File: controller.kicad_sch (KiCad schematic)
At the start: 33 parts, among them J10 07x01_2.54mm_Header, J4 03x01_2.54mm_Header, J6 03x01_2.54mm_Header, J9 07x01_2.54mm_Header, U4 STM32H742VGT6

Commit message: updates components to latest library. Refs: #30
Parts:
- U4: footprint Package_QFP:LQFP-100_14x14mm_P0.5mm -> KL_Footprints:LQFP-100_14x14mm_P0.5mm
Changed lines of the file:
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@@
 		(on_board yes)
 		(dnp no)
+		(fields_autoplaced yes)
 		(property "Reference" "J4"
-			(at 190.246 74.676 0)
+			(at 190.5 63.5 0)
 			(effects
 				(font
@@
 			)
 		)
-		(property "Dielectric" ""
-			(at 69.85 133.35 90)
-			(effects
-				(font
-					(size 1.27 1.27)
-				)
-				(hide yes)
-			)
-		)
-		(property "Dielectric_type" ""
-			(at 69.85 133.35 90)
-			(effects
-				(font
-					(size 1.27 1.27)
-				)
-				(hide yes)
-			)
-		)
-		(property "LSCS" ""
-			(at 69.85 133.35 90)
-			(effects
-				(font
-					(size 1.27 1.27)
-				)
-				(hide yes)
-			)
-		)
-		(property "Max Current" ""
-			(at 69.85 133.35 90)
-			(effects
-				(font
-					(size 1.27 1.27)
-				)
-				(hide yes)
-			)
-		)
 		(pin "2"
 		)
@@
 		(fields_autoplaced yes)
 		(property "Reference" "J10"
-			(at 214.63 67.31 0)
+			(at 212.09 77.7874 0)
 			(effects
 				(font
 					(size 1.27 1.27)
 				)
+				(justify left)
 			)
 		)
@@
 			)
 		)
-		(property "Dielectric" ""
-			(at 69.85 148.59 90)
-			(effects
-				(font
-					(size 1.27 1.27)
-				)
-				(hide yes)
-			)
-		)
-		(property "Dielectric_type" ""
-			(at 69.85 148.59 90)
-			(effects
-				(font
-					(size 1.27 1.27)
-				)
-				(hide yes)
-			)
-		)
-		(property "LSCS" ""
-			(at 69.85 148.59 90)
-			(effects
-				(font
-					(size 1.27 1.27)
-				)
-				(hide yes)
-			)
-		)
-		(property "Max Current" ""
-			(at 69.85 148.59 90)
-			(effects
-				(font
-					(size 1.27 1.27)
-				)
-				(hide yes)
-			)
-		)
 		(pin "2"
 		)
@@
 		)
 		(property "LABEL" "${REFERENCE}:${COLOR}"
-			(at 58.42 129.794 0)
+			(at 58.166 135.89 0)
 			(effects
 				(font
@@
 		)
 		(property "LABEL" "${REFERENCE}:${COLOR}"
-			(at 58.42 144.78 0)
+			(at 58.166 151.13 0)
 			(effects
 				(font
@@
 			)
 		)
-		(property "Footprint" "Package_QFP:LQFP-100_14x14mm_P0.5mm"
+		(property "Footprint" "KL_Footprints:LQFP-100_14x14mm_P0.5mm"
 			(at 83.82 173.99 0)
 			(effects
@@
 		(fields_autoplaced yes)
 		(property "Reference" "J9"
-			(at 214.63 48.26 0)
+			(at 212.09 58.7374 0)
 			(effects
 				(font
 					(size 1.27 1.27)
 				)
+				(justify left)
 			)
 		)
@@
 		(dnp no)
 		(fields_autoplaced yes)
-		(property "Reference" "#PWR095"
+		(property "Reference" "#PWR95"
 			(at 45.72 144.78 0)
 			(effects
@@
 			(project ""
 				(path "/d4536448-b109-4159-96e2-3dc21baf2d6e/06488c82-a47f-4277-b0ee-3bd211d8922a"
-					(reference "#PWR095")
+					(reference "#PWR95")
 					(unit 1)
 				)
@@
 		)
 		(property "LABEL" "${REFERENCE}:${COLOR}"
-			(at 58.42 137.16 0)
+			(at 58.166 143.51 0)
 			(effects
 				(font
@@
 			(effects
 				(font
-					(size 1.27 1.27)
-				)
-				(hide yes)
-			)
-		)
-		(property "Dielectric" ""
-			(at 69.85 140.97 90)
-			(effects
-				(font
-					(size 1.27 1.27)
-				)
-				(hide yes)
-			)
-		)
-		(property "Dielectric_type" ""
-			(at 69.85 140.97 90)
-			(effects
-				(font
-					(size 1.27 1.27)
-				)
-				(hide yes)
-			)
-		)
-		(property "LSCS" ""
-			(at 69.85 140.97 90)
-			(effects
-				(font
-					(size 1.27 1.27)
-				)
-				(hide yes)
-			)
-		)
-		(property "Max Current" ""
-			(at 69.85 140.97 90)
-			(effects
-				(font

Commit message: open project in KiCAD10. Refs: #41
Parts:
- TP23, TP32, TP33, TP34, TP35: value ~ -> (none)

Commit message: updates controller. Refs: #41
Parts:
- C104, C77, C78, C85, C93, C94, C95: symbol KL_C:C_100n_10V_X7R_0603_10 -> KL_C:C_100n_10V_10pct_X7R_0603; Dielectric (none) -> X7R; MPN (none) -> CC0603KRX7R6BB104; Package_in_inch (none) -> 0603; Tolerance 10 -> (none); Tolerance_in_pct (none) -> 10; Voltage 50 -> (none); Voltage_in_V (none) -> 10
- C105: symbol KL_C:C_4u7_10V_X5R_0603_10 -> KL_C:C_4u7_10V_10pct_X5R_0603; Dielectric (none) -> X5R; MPN (none) -> C0603C475K8PAC7411; Package_in_inch (none) -> 0603; Tolerance 10 -> (none); Tolerance_in_pct (none) -> 10; Voltage 10 -> (none); Voltage_in_V (none) -> 10
- C81, C82, C83, C84: symbol KL_C:C_2u2_10V_Y5V_0603_20 -> KL_C:C_2u2_10V_20pct_Y5V_0603; Dielectric (none) -> Y5V; MPN (none) -> EMK107BJ225KA-T; Package_in_inch (none) -> 0603; Tolerance 10 -> (none); Tolerance_in_pct (none) -> 20; Voltage 16 -> (none); Voltage_in_V (none) -> 10
- D4: symbol KL_LED:LED_green_2V1_0.03A -> KL_LED:LED_Green_2.1V_0.03A_0603; MPN (none) -> LTST-C190GKT; Package_in_inch (none) -> 0603
- D5: symbol KL_LED:LED_orange_2V_0.03A -> KL_LED:LED_Orange_2V_0.03A_0603; MPN (none) -> LTST-C190KFKT; Package_in_inch (none) -> 0603
- D6: symbol KL_LED:LED_red_2V_0.03A -> KL_LED:LED_Red_2V_0.03A_0603; MPN (none) -> LTST-C194KRKT; Package_in_inch (none) -> 0603
- J10, J9: value 07x01_2.54mm_Header -> Header_07x01_2.54mm_0mm_Straight; symbol KL_Headers:07x01_2.54mm_Header -> KL_Header:Header_07x01_2.54mm_0mm_Straight; MPN (none) -> TLW-107-06-G-S; No_of_pins (none) -> 7; No_of_rows (none) -> 1; Orientation (none) -> Straight; Pitch_pin_in_mm (none) -> 2.54; Pitch_row_in_mm (none) -> 0
- J4, J6: value 03x01_2.54mm_Header -> Header_03x01_2.54mm_0mm_Straight; symbol KL_Headers:03x01_2.54mm_Header -> KL_Header:Header_03x01_2.54mm_0mm_Straight; MPN (none) -> 87224-3; No_of_pins (none) -> 3; No_of_rows (none) -> 1; Orientation (none) -> Straight; Pitch_pin_in_mm (none) -> 2.54; Pitch_row_in_mm (none) -> 0
- R102: symbol KL_R:R_10K_100mW_5_0603 -> KL_R:R_10K_0.1W_5pct_0603; MPN (none) -> CRCW060310K0JNEC; Package (in) 0603 -> (none); Package_in_inch (none) -> 0603; Power 100mW -> (none); Power_in_W (none) -> 0.1; Tolerance 5% -> (none); Tolerance_in_pct (none) -> 5
- R108: symbol KL_R:R_0R_2W_5_2512 -> KL_R:R_0R_2W_5pct_2512; MPN (none) -> CRF2512-J/-000ELF; Mouser 652-CRF2512-J-000ELF -> 652-CRF2512-J-000ELF; Package (in) 2512 -> (none); Package_in_inch (none) -> 2512; Power 2 -> (none); Power_in_W (none) -> 2; Tolerance 5 -> (none); Tolerance_in_pct (none) -> 5
- R110, R111, R74: value 22 -> 22R; symbol KL_R:R_22_100mW_1pct_0603 -> KL_R:R_22R_0.1W_1pct_0603; MPN (none) -> RC0603FR-1022RL; Package (in) 0603 -> (none); Package_in_inch (none) -> 0603; Power 0.1 -> (none); Power_in_W (none) -> 0.1; Tolerance 1 -> (none); Tolerance_in_pct (none) -> 1
- R137, R87, R89: symbol KL_R:R_1K5_100mW_5_0603 -> KL_R:R_1K5_0.1W_5pct_0603; MPN (none) -> AC0603JR-071K5L; Package (in) 0603 -> (none); Package_in_inch (none) -> 0603; Power 0.1 -> (none); Power_in_W (none) -> 0.1; Tolerance 5 -> (none); Tolerance_in_pct (none) -> 5
- TP23, TP32, TP33, TP34, TP35: footprint Connector_PinHeader_2.54mm:PinHeader_1x01_P2.54mm_Vertical -> KL_Footprints:TestPoint; symbol KL_TP:TestPoint -> KL_TestPoint:TestPoint
- U4: MPN (none) -> STM32H742VGT6; V_DD_max_V (none) -> 4

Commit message: updates 2u2 capacitors. Refs: #41
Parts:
- C81, C82, C83, C84: symbol KL_C:C_2u2_10V_20pct_Y5V_0603 -> KL_C:C_2u2_35V_20pct_X5R_0603; Dielectric Y5V -> X5R; Digikey 587-1430-1-ND -> 490-10486-1-ND; LCSC C76612 -> C710921; MPN EMK107BJ225KA-T -> GRM188R6YA225MA12D; Mouser 963-EMK107BJ225KA-T -> 81-GRM188R6YA225MA2D; Voltage_in_V 10 -> 35
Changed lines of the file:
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@@
 	)
 	(symbol
-		(lib_id "KL_C:C_2u2_10V_20pct_Y5V_0603")
+		(lib_id "KL_C:C_2u2_35V_20pct_X5R_0603")
 		(at 29.21 173.99 90)
 		(unit 1)
@@
 			)
 		)
-		(property "Datasheet" "file:///home/alex/Downloads/MLASE168SB5225KTNA01_SS.pdf"
+		(property "Datasheet" "https://search.murata.co.jp/Ceramy/image/img/A01X/G101/ENG/GRM188R6YA225MA12-01.pdf"
 			(at 29.21 173.99 0)
 			(hide yes)
@@
 			)
 		)
-		(property "Mouser" "963-EMK107BJ225KA-T"
+		(property "Mouser" "81-GRM188R6YA225MA2D"
 			(at 29.21 173.99 0)
 			(hide yes)
@@
 			)
 		)
-		(property "Digikey" "587-1430-1-ND"
+		(property "Digikey" "490-10486-1-ND"
 			(at 29.21 173.99 0)
 			(hide yes)
@@
 			)
 		)
-		(property "LCSC" "C76612"
+		(property "LCSC" "C710921"
 			(at 29.21 173.99 0)
 			(hide yes)
@@
 			)
 		)
-		(property "Voltage_in_V" "10"
+		(property "Voltage_in_V" "35"
 			(at 29.21 173.99 0)
 			(hide yes)
@@
 			)
 		)
-		(property "Dielectric" "Y5V"
+		(property "Dielectric" "X5R"
 			(at 29.21 173.99 0)
 			(hide yes)
@@
 			)
 		)
-		(property "MPN" "EMK107BJ225KA-T"
+		(property "MPN" "GRM188R6YA225MA12D"
 			(at 29.21 173.99 0)
 			(hide yes)
@@
 	)
 	(symbol
-		(lib_id "KL_C:C_2u2_10V_20pct_Y5V_0603")
+		(lib_id "KL_C:C_2u2_35V_20pct_X5R_0603")
 		(at 29.21 162.56 90)
 		(unit 1)
@@
 			)
 		)
-		(property "Datasheet" "file:///home/alex/Downloads/MLASE168SB5225KTNA01_SS.pdf"
+		(property "Datasheet" "https://search.murata.co.jp/Ceramy/image/img/A01X/G101/ENG/GRM188R6YA225MA12-01.pdf"
 			(at 29.21 162.56 0)
 			(hide yes)
@@
 			)
 		)
-		(property "Mouser" "963-EMK107BJ225KA-T"
+		(property "Mouser" "81-GRM188R6YA225MA2D"
 			(at 29.21 162.56 0)
 			(hide yes)
@@
 			)
 		)
-		(property "Digikey" "587-1430-1-ND"
+		(property "Digikey" "490-10486-1-ND"
 			(at 29.21 162.56 0)
 			(hide yes)
@@
 			)
 		)
-		(property "LCSC" "C76612"
+		(property "LCSC" "C710921"
 			(at 29.21 162.56 0)
 			(hide yes)
@@
 			)
 		)
-		(property "Voltage_in_V" "10"
+		(property "Voltage_in_V" "35"
 			(at 29.21 162.56 0)
 			(hide yes)
@@
 			)
 		)
-		(property "Dielectric" "Y5V"
+		(property "Dielectric" "X5R"
 			(at 29.21 162.56 0)
 			(hide yes)
@@
 			)
 		)
-		(property "MPN" "EMK107BJ225KA-T"
+		(property "MPN" "GRM188R6YA225MA12D"
 			(at 29.21 162.56 0)
 			(hide yes)
@@
 	)
 	(symbol
-		(lib_id "KL_C:C_2u2_10V_20pct_Y5V_0603")
+		(lib_id "KL_C:C_2u2_35V_20pct_X5R_0603")
 		(at 29.21 139.7 90)
 		(unit 1)
@@
 			)
 		)
-		(property "Datasheet" "file:///home/alex/Downloads/MLASE168SB5225KTNA01_SS.pdf"
+		(property "Datasheet" "https://search.murata.co.jp/Ceramy/image/img/A01X/G101/ENG/GRM188R6YA225MA12-01.pdf"
 			(at 29.21 139.7 0)
 			(hide yes)
@@
 			)
 		)
-		(property "Mouser" "963-EMK107BJ225KA-T"
+		(property "Mouser" "81-GRM188R6YA225MA2D"
 			(at 29.21 139.7 0)
 			(hide yes)
@@
 			)
 		)
-		(property "Digikey" "587-1430-1-ND"
+		(property "Digikey" "490-10486-1-ND"
 			(at 29.21 139.7 0)
 			(hide yes)
@@
 			)
 		)
-		(property "LCSC" "C76612"
+		(property "LCSC" "C710921"
 			(at 29.21 139.7 0)
 			(hide yes)
@@
 			)
 		)
-		(property "Voltage_in_V" "10"
+		(property "Voltage_in_V" "35"
 			(at 29.21 139.7 0)
 			(hide yes)
@@
 			)
 		)
-		(property "Dielectric" "Y5V"
+		(property "Dielectric" "X5R"
 			(at 29.21 139.7 0)
 			(hide yes)
@@
 			)
 		)
-		(property "MPN" "EMK107BJ225KA-T"
+		(property "MPN" "GRM188R6YA225MA12D"
 			(at 29.21 139.7 0)
 			(hide yes)
@@
 	)
 	(symbol
-		(lib_id "KL_C:C_2u2_10V_20pct_Y5V_0603")
+		(lib_id "KL_C:C_2u2_35V_20pct_X5R_0603")
 		(at 29.21 151.13 90)
 		(unit 1)
@@
 			)
 		)
-		(property "Datasheet" "file:///home/alex/Downloads/MLASE168SB5225KTNA01_SS.pdf"
+		(property "Datasheet" "https://search.murata.co.jp/Ceramy/image/img/A01X/G101/ENG/GRM188R6YA225MA12-01.pdf"
 			(at 29.21 151.13 0)
 			(hide yes)
@@
 			)
 		)
-		(property "Mouser" "963-EMK107BJ225KA-T"
+		(property "Mouser" "81-GRM188R6YA225MA2D"
 			(at 29.21 151.13 0)
 			(hide yes)
@@
 			)
 		)
-		(property "Digikey" "587-1430-1-ND"
+		(property "Digikey" "490-10486-1-ND"
 			(at 29.21 151.13 0)
 			(hide yes)
@@
 			)
 		)
-		(property "LCSC" "C76612"
+		(property "LCSC" "C710921"
 			(at 29.21 151.13 0)
 			(hide yes)
@@
 			)
 		)
-		(property "Voltage_in_V" "10"
+		(property "Voltage_in_V" "35"
 			(at 29.21 151.13 0)
 			(hide yes)
@@
 			)
 		)
-		(property "Dielectric" "Y5V"
+		(property "Dielectric" "X5R"
 			(at 29.21 151.13 0)
 			(hide yes)
@@
 			)
 		)
-		(property "MPN" "EMK107BJ225KA-T"
+		(property "MPN" "GRM188R6YA225MA12D"
 			(at 29.21 151.13 0)
 			(hide yes)

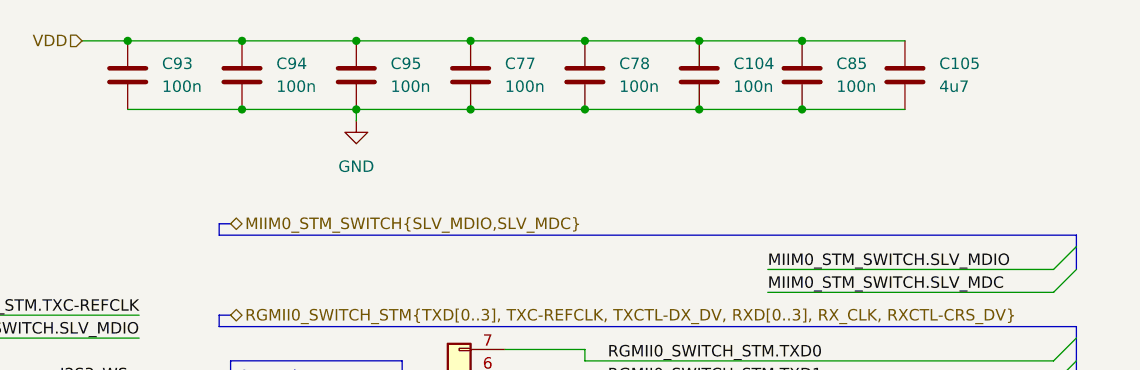
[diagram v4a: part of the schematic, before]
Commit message: replaces all capacitors with 10u. Refs: #52
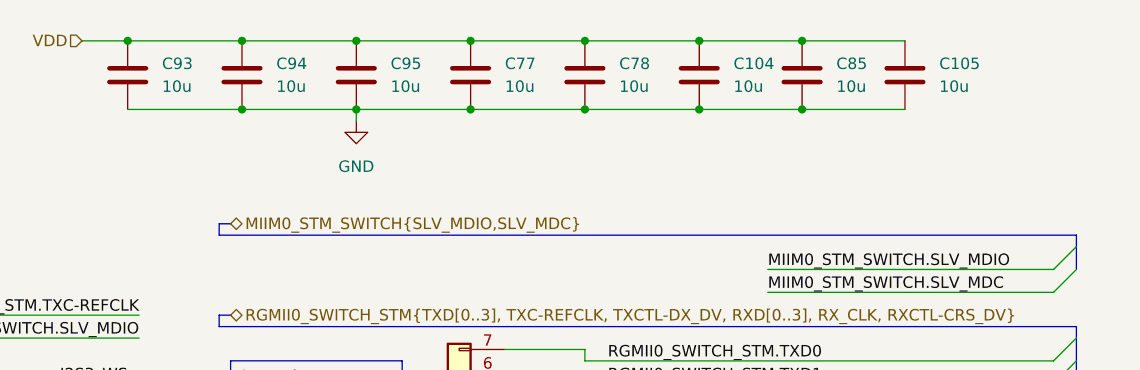
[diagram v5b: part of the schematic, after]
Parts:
- C104, C77, C78, C85, C93, C94, C95: value 100n -> 10u; symbol KL_C:C_100n_10V_10pct_X7R_0603 -> KL_C:C_10u_25V_20pct_X5R_0603; Dielectric X7R -> X5R; Digikey 311-4055-1-ND -> 1276-1869-1-ND; LCSC C519438 -> C96446; MPN CC0603KRX7R6BB104 -> CL10A106MA8NRNC; Mouser 603-CC603KRX7R6BB104 -> 187-CL10A106MA8NRNC; Tolerance_in_pct 10 -> 20; Voltage_in_V 10 -> 25
- C105: value 4u7 -> 10u; symbol KL_C:C_4u7_10V_10pct_X5R_0603 -> KL_C:C_10u_25V_20pct_X5R_0603; Digikey 399-C0603C475K8PACTUCT-ND -> 1276-1869-1-ND; LCSC C5177163 -> C96446; MPN C0603C475K8PAC7411 -> CL10A106MA8NRNC; Mouser 80-C0603C475K8PACLR -> 187-CL10A106MA8NRNC; Tolerance_in_pct 10 -> 20; Voltage_in_V 10 -> 25

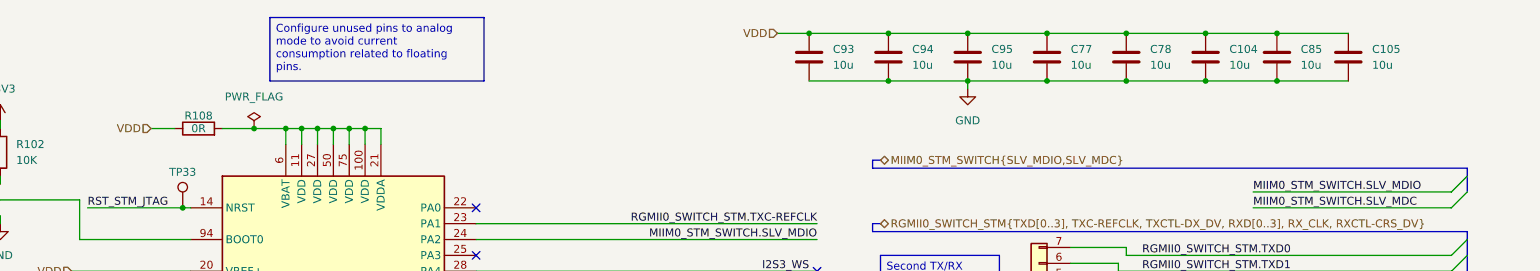
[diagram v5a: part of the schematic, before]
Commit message: moves 0R resistor in front of buffering caps. Refs: #57
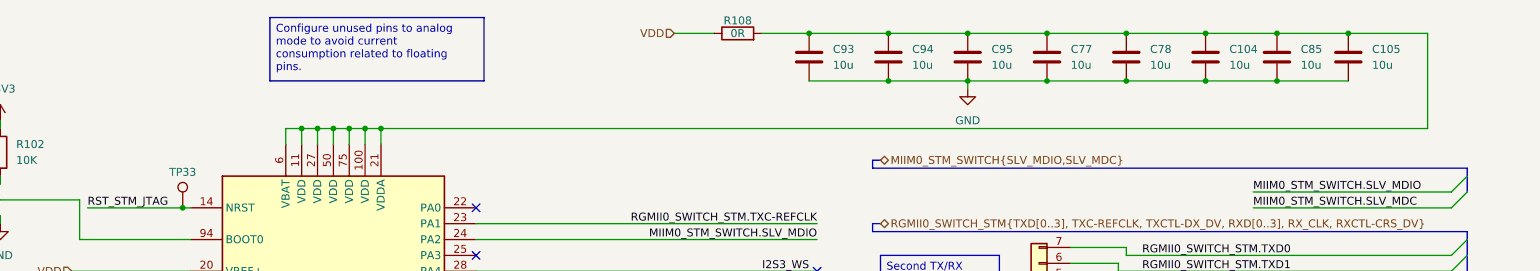
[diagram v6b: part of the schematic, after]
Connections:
- net VDD: no longer C104.1, C105.1, C77.1, C78.1, C85.1, C93.1, C94.1, C95.1
- net at R108.2, U4.100 (VDD), U4.11 (VDD)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: now also C104.1, C105.1, C77.1, C78.1, C85.1, C93.1, C94.1, C95.1
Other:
- moved on the sheet: R108
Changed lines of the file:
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@@
 	)
 	(junction
+		(at 177.8 16.51)
+		(diameter 0)
+		(color 0 0 0 0)
+	)
+	(junction
 		(at 99.06 181.61)
 		(diameter 0)
@@
 	)
 	(junction
+		(at 264.16 16.51)
+		(diameter 0)
+		(color 0 0 0 0)
+	)
+	(junction
 		(at 215.9 16.51)
 		(diameter 0)
@@
 	)
 	(junction
-		(at 177.8 16.51)
-		(diameter 0)
-		(color 0 0 0 0)
-	)
-	(junction
 		(at 228.6 16.51)
 		(diameter 0)
@@
 	)
 	(junction
-		(at 93.98 31.75)
+		(at 109.22 31.75)
 		(diameter 0)
 		(color 0 0 0 0)
@@
 	)
 	(junction
-		(at 88.9 31.75)
-		(diameter 0)
-		(color 0 0 0 0)
-	)
-	(junction
 		(at 101.6 31.75)
 		(diameter 0)
@@
 	(wire
 		(pts
+			(xy 109.22 31.75) (xy 276.86 31.75)
+		)
+		(stroke
+			(width 0)
+			(type default)
+		)
+	)
+	(wire
+		(pts
 			(xy 248.92 41.91) (xy 280.67 41.91)
 		)
@@
 	(wire
 		(pts
+			(xy 276.86 16.51) (xy 264.16 16.51)
+		)
+		(stroke
+			(width 0)
+			(type default)
+		)
+	)
+	(wire
+		(pts
 			(xy 78.74 156.21) (xy 33.02 156.21)
 		)
@@
 	(wire
 		(pts
-			(xy 72.39 31.75) (xy 76.2 31.75)
-		)
-		(stroke
-			(width 0)
-			(type default)
-		)
-	)
-	(wire
-		(pts
 			(xy 124.46 74.93) (xy 180.34 74.93)
 		)
@@
 	(wire
 		(pts
+			(xy 276.86 31.75) (xy 276.86 16.51)
+		)
+		(stroke
+			(width 0)
+			(type default)
+		)
+	)
+	(wire
+		(pts
 			(xy 124.46 140.97) (xy 179.07 140.97)
 		)
@@
 	(wire
 		(pts
+			(xy 170.18 16.51) (xy 177.8 16.51)
+		)
+		(stroke
+			(width 0)
+			(type default)
+		)
+	)
+	(wire
+		(pts
 			(xy 222.25 133.35) (xy 248.92 133.35)
 		)
@@
 	(wire
 		(pts
-			(xy 172.72 16.51) (xy 177.8 16.51)
+			(xy 156.21 16.51) (xy 162.56 16.51)
 		)
 		(stroke
@@
 	(wire
 		(pts
-			(xy 83.82 31.75) (xy 88.9 31.75)
-		)
-		(stroke
-			(width 0)
-			(type default)
-		)
-	)
-	(wire
-		(pts
 			(xy 219.71 66.04) (xy 220.98 66.04)
 		)
@@
 		)
 	)
-	(wire
-		(pts
-			(xy 88.9 31.75) (xy 93.98 31.75)
-		)
-		(stroke
-			(width 0)
-			(type default)
-		)
-	)
 	(bus
 		(pts
@@
 	(hierarchical_label "VDD"
 		(shape input)
-		(at 172.72 16.51 180)
+		(at 156.21 16.51 180)
 		(effects
 			(font
@@
 		)
 	)
-	(hierarchical_label "VDD"
-		(shape input)
-		(at 72.39 31.75 180)
-		(effects
-			(font
-				(size 1.27 1.27)
-			)
-			(justify right)
-		)
-	)
 	(hierarchical_label "EN-1V15_STM_TO_BUCK"
 		(shape output)
@@
 	)
 	(symbol
-		(lib_id "KL_Flags:PWR_FLAG")
-		(at 88.9 31.75 0)
-		(unit 1)
-		(body_style 1)
-		(exclude_from_sim no)
-		(in_bom yes)
-		(on_board yes)
-		(in_pos_files yes)
-		(dnp no)
-		(fields_autoplaced yes)
-		(property "Reference" "#FLG6"
-			(at 88.9 29.845 0)
-			(hide yes)
-			(show_name no)
-			(do_not_autoplace no)
-			(effects
-				(font
-					(size 1.27 1.27)
-				)
-			)
-		)
-		(property "Value" "PWR_FLAG"
-			(at 88.9 26.67 0)
-			(show_name no)
-			(do_not_autoplace no)
-			(effects
-				(font
-					(size 1.27 1.27)
-				)
-			)
-		)
-		(property "Footprint" ""
-			(at 88.9 31.75 0)
-			(hide yes)
-			(show_name no)
-			(do_not_autoplace no)
-			(effects
-				(font
-					(size 1.27 1.27)
-				)
-			)
-		)
-		(property "Datasheet" ""
-			(at 88.9 31.75 0)
-			(hide yes)
-			(show_name no)
-			(do_not_autoplace no)
-			(effects
-				(font
-					(size 1.27 1.27)
-				)
-			)
-		)
-		(property "Description" "Special symbol for telling ERC where power comes from"
-			(at 88.9 31.75 0)
-			(hide yes)
-			(show_name no)
-			(do_not_autoplace no)
-			(effects
-				(font
-					(size 1.27 1.27)
-				)
-			)
-		)
-		(pin "1"
-		)
-		(instances
-			(project "shish-lan"
-				(path "/d4536448-b109-4159-96e2-3dc21baf2d6e/06488c82-a47f-4277-b0ee-3bd211d8922a"
-					(reference "#FLG6")
-					(unit 1)
-				)
-			)
-		)
-	)
-	(symbol
 		(lib_id "KL_TestPoint:TestPoint")
 		(at 41.91 113.03 0)
@@
 	(symbol
 		(lib_id "KL_R:R_0R_2W_5pct_2512")
-		(at 80.01 31.75 90)
+		(at 166.37 16.51 90)
 		(unit 1)
 		(body_style 1)
@@
 		(dnp no)
 		(property "Reference" "R108"
-			(at 80.01 29.718 90)
+			(at 166.37 14.478 90)
 			(show_name no)
 			(do_not_autoplace no)
@@
 		)
 		(property "Value" "0R"
-			(at 80.01 31.75 90)
+			(at 166.37 16.51 90)
 			(show_name no)
 			(do_not_autoplace no)
@@
 		)
 		(property "Footprint" "KL_Footprints:R_2512"
-			(at 80.01 33.528 90)
+			(at 166.37 18.288 90)
 			(hide yes)
 			(show_name no)
@@
 		)
 		(property "Datasheet" "https://www.bourns.com/docs/Product-Datasheets/CRF-J.pdf"
-			(at 80.01 31.75 0)
+			(at 166.37 16.51 0)
 			(hide yes)
 			(show_name no)
@@
 		)
 		(property "Description" "Resistor"
-			(at 80.01 31.75 0)
+			(at 166.37 16.51 0)
 			(hide yes)
 			(show_name no)
@@
 		)
 		(property "Mouser" "652-CRF2512-J-000ELF"
-			(at 80.01 31.75 0)
+			(at 166.37 16.51 0)
 			(hide yes)
 			(show_name no)
@@
 		)
 		(property "Digikey" "118-CRF2512-J/-000ELFCT-ND"
-			(at 80.01 31.75 0)
+			(at 166.37 16.51 0)
 			(hide yes)
 			(show_name no)
@@
 		)
 		(property "LCSC" "C2778666"
-			(at 80.01 31.75 0)
+			(at 166.37 16.51 0)
 			(hide yes)
 			(show_name no)
@@
 		)
 		(property "Power_in_W" "2"
-			(at 80.01 31.75 0)
+			(at 166.37 16.51 0)
 			(hide yes)
 			(show_name no)
@@
 		)
 		(property "Tolerance_in_pct" "5"
-			(at 80.01 31.75 0)
+			(at 166.37 16.51 0)
 			(hide yes)
 			(show_name no)
@@
 		)
 		(property "MPN" "CRF2512-J/-000ELF"
-			(at 80.01 31.75 0)
+			(at 166.37 16.51 0)
 			(hide yes)
 			(show_name no)
@@
 		)
 		(property "Package_in_inch" "2512"
-			(at 80.01 31.75 0)
+			(at 166.37 16.51 0)
 			(hide yes)
 			(show_name no)
